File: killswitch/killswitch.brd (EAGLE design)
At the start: 42.3 x 42.3 mm, 32 parts, among them U1 CD4012BPWR, U2 2N7002-7-F

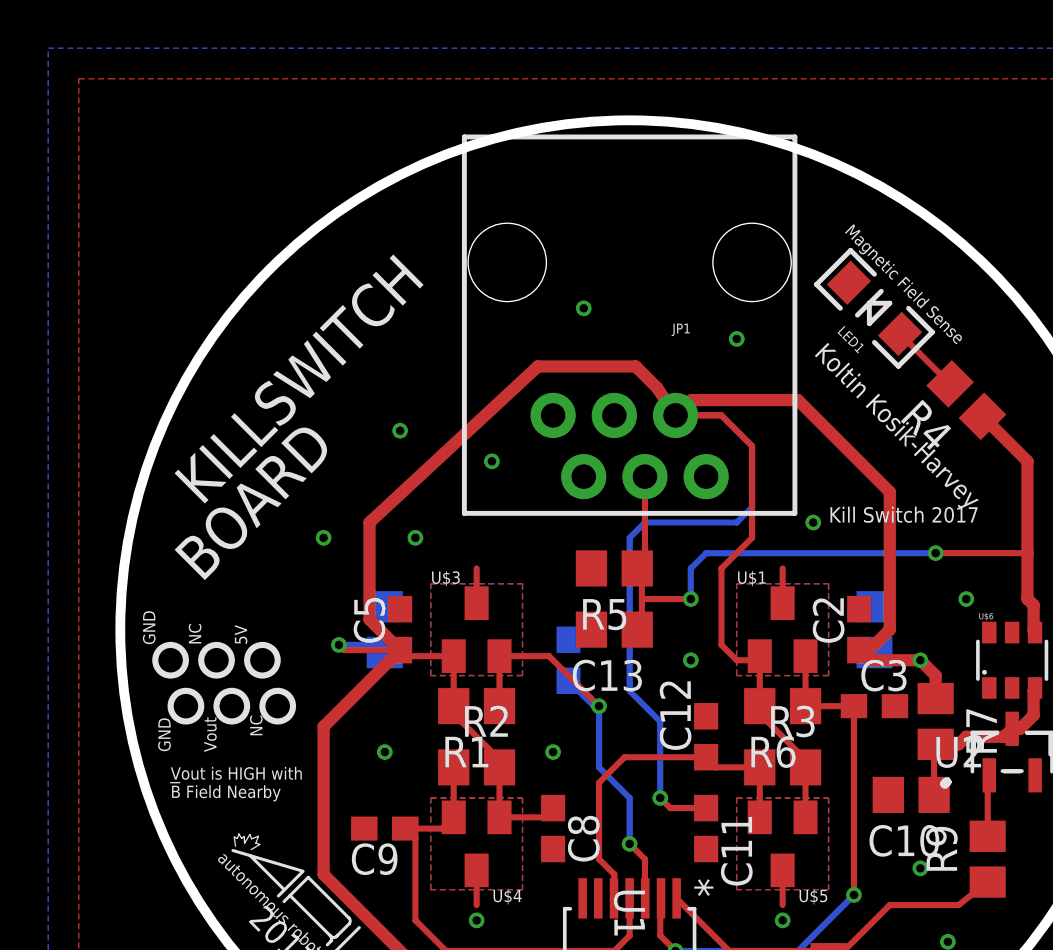
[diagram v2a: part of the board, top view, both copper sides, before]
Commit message: Removed RJ11 and replaced with 3-pin Header
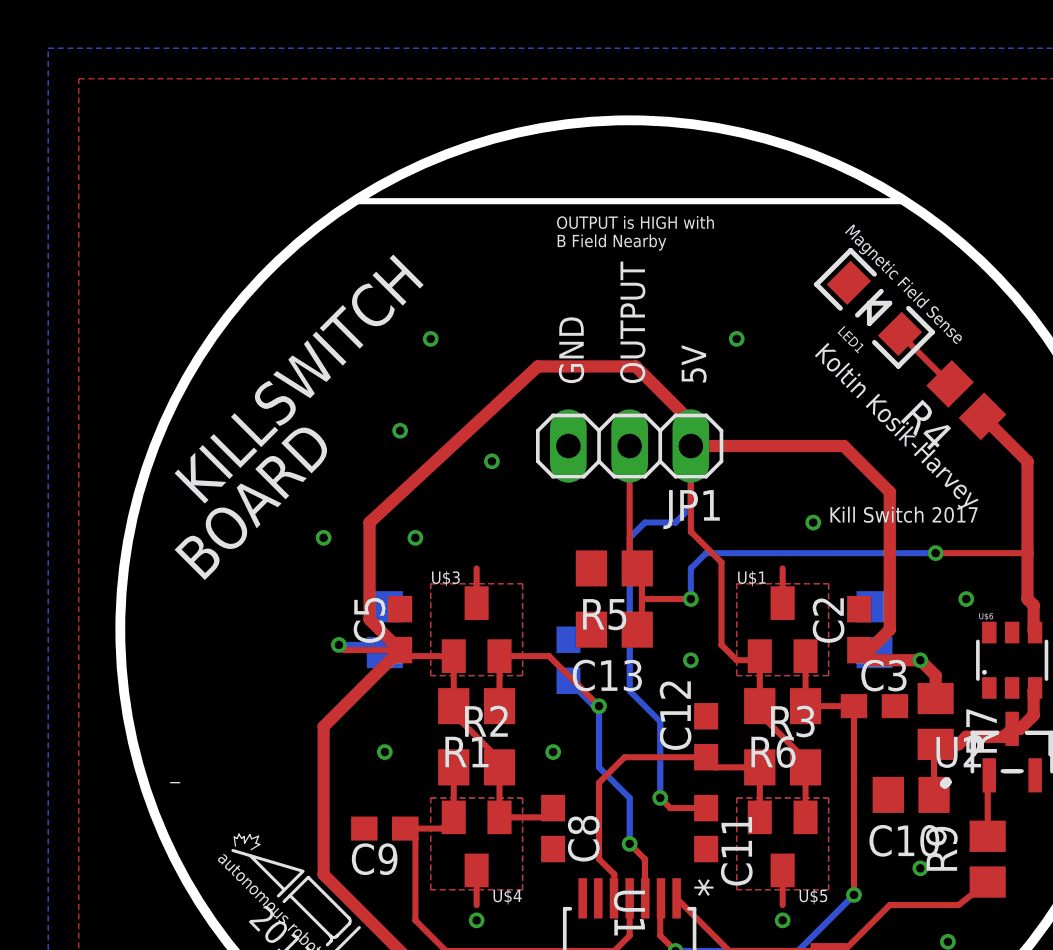
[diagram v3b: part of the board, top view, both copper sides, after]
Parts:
- JP1: value RJ11 -> (none); device SparkFun-Connectors:RJ11-6 -> pinhead:1X03
- moved JP1 7.62 mm to (20.3, 25.4)
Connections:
- net +5V: now also JP1.1; no longer JP1.2
- net GND: now also JP1.3; no longer JP1.5, JP1.6
- net OUTPUT: now also JP1.2; no longer JP1.3
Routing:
- net +5V: track 144.1 -> 134.1 mm
- net OUTPUT: track 34.5 -> 35.8 mm
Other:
- outline, holes or cut-outs redrawn
- board text added: "OUTPUT"
- board text added: "OUTPUT is HIGH with B Field Nearby"
- board text removed: "NC"
- board text removed: "Vout"
- board text removed: "Vout is HIGH with B Field Nearby"
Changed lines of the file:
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@@
 <text x="2.54" y="22.86" size="1.778" layer="21" font="vector" rot="R45">KILLSWITCH</text>
 <text x="2.54" y="19.685" size="1.778" layer="21" font="vector" rot="R45">BOARD</text>
-<circle x="1.27" y="16.51" radius="0.635" width="0.254" layer="21"/>
-<circle x="3.175" y="16.51" radius="0.635" width="0.254" layer="21"/>
-<circle x="5.08" y="16.51" radius="0.635" width="0.254" layer="21"/>
-<circle x="1.905" y="14.605" radius="0.635" width="0.254" layer="21"/>
-<circle x="3.81" y="14.605" radius="0.635" width="0.254" layer="21"/>
-<circle x="5.715" y="14.605" radius="0.635" width="0.254" layer="21"/>
-<text x="2.54" y="17.145" size="0.508" layer="21" rot="R90">NC</text>
-<text x="0.635" y="17.145" size="0.508" layer="21" rot="R90">GND</text>
-<text x="4.445" y="17.145" size="0.508" layer="21" rot="R90">5V</text>
-<text x="1.27" y="12.7" size="0.508" layer="21" rot="R90">GND</text>
-<text x="3.175" y="12.7" size="0.508" layer="21" rot="R90">Vout</text>
-<text x="5.08" y="13.335" size="0.508" layer="21" rot="R90">NC</text>
-<text x="1.27" y="10.795" size="0.508" layer="21">Vout is HIGH with
+<text x="23.495" y="27.94" size="1.016" layer="21" rot="R90">5V</text>
+<text x="18.415" y="27.94" size="1.016" layer="21" rot="R90">GND</text>
+<text x="20.955" y="27.94" size="1.016" layer="21" rot="R90">OUTPUT</text>
+<text x="17.272" y="33.655" size="0.508" layer="21">OUTPUT is HIGH with
 B Field Nearby</text>
 <wire x1="1.27" y1="11.43" x2="1.651" y2="11.43" width="0.0508" layer="21"/>
 <text x="29.21" y="34.29" size="0.508" layer="21" rot="R315">Magnetic Field Sense</text>
+<wire x1="8.89" y1="35.56" x2="31.75" y2="35.56" width="0.254" layer="20"/>
 </plain>
 <attributes>
@@
 </autorouter>
 <elements>
-<element name="JP1" library="SparkFun-Connectors" package="RJ11-6" value="RJ11" x="20.32" y="33.02" rot="R180">
-<attribute name="PROD_ID" value="CONN-08590" x="20.32" y="33.02" size="1.778" layer="27" rot="R180" display="off"/>
-<attribute name="VALUE" value="RJ11" x="20.32" y="33.02" size="1.778" layer="27" rot="R180" display="off"/>
-</element>
 <element name="U$2" library="ARVP" package="LOGO2" value="" x="3.175" y="8.255" smashed="yes" rot="R315"/>
 <element name="U$1" library="KillSwitch" library_urn="urn:adsk.eagle:library:576207" package="SOT23" value="TCS40DLR" x="26.67" y="17.78"/>
@@
 <element name="R9" library="resistor" library_urn="urn:adsk.eagle:library:348" package="R0805" package3d_urn="urn:adsk.eagle:package:26059/1" value="1k" x="35.179" y="8.255" rot="R90"/>
 <element name="C10" library="resistor" library_urn="urn:adsk.eagle:library:348" package="C0805" package3d_urn="urn:adsk.eagle:package:26137/1" value="100nF" x="32.004" y="10.922" rot="R180"/>
+<element name="JP1" library="pinhead" library_urn="urn:adsk.eagle:library:325" package="1X03" package3d_urn="urn:adsk.eagle:package:22458/2" value="" x="20.32" y="25.4" rot="R180"/>
 </elements>
 <signals>
 <signal name="GND">
-<contactref element="JP1" pad="5"/>
-<contactref element="JP1" pad="6"/>
 <contactref element="U$1" pad="GND"/>
 <contactref element="C1" pad="2"/>
@@
 <wire x1="26.67" y1="7.79" x2="26.67" y2="6.35" width="0.254" layer="1"/>
 <via x="11.43" y="21.59" extent="1-16" drill="0.35"/>
-<via x="18.415" y="31.115" extent="1-16" drill="0.35"/>
+<via x="12.065" y="29.845" extent="1-16" drill="0.35"/>
 <via x="27.94" y="22.225" extent="1-16" drill="0.35"/>
 <via x="38.735" y="21.59" extent="1-16" drill="0.35"/>
@@
 <contactref element="C13" pad="2"/>
 <contactref element="C10" pad="2"/>
+<contactref element="JP1" pad="3"/>
 </signal>
 <signal name="+5V">
-<contactref element="JP1" pad="2"/>
 <contactref element="U$1" pad="VCC"/>
 <contactref element="C1" pad="1"/>
@@
 <wire x1="25.72" y1="16.51" x2="25.72" y2="14.605" width="0.254" layer="1"/>
 <wire x1="25.72" y1="16.51" x2="25.72" y2="16.68" width="0.254" layer="1"/>
-<wire x1="22.225" y1="26.67" x2="24.13" y2="26.67" width="0.254" layer="1"/>
-<wire x1="24.13" y1="26.67" x2="25.4" y2="25.4" width="0.254" layer="1"/>
-<wire x1="25.4" y1="25.4" x2="25.4" y2="21.59" width="0.254" layer="1"/>
-<wire x1="25.4" y1="21.59" x2="24.13" y2="20.32" width="0.254" layer="1"/>
-<wire x1="24.13" y1="20.32" x2="24.13" y2="17.145" width="0.254" layer="1"/>
-<wire x1="24.13" y1="17.145" x2="24.765" y2="16.51" width="0.254" layer="1"/>
+<wire x1="24.765" y1="16.51" x2="24.13" y2="17.145" width="0.254" layer="1"/>
 <wire x1="24.765" y1="16.51" x2="25.72" y2="16.51" width="0.254" layer="1"/>
 <wire x1="27.62" y1="12.065" x2="27.62" y2="9.99" width="0.254" layer="1"/>
-<wire x1="22.225" y1="26.67" x2="21.463" y2="27.813" width="0.508" layer="1"/>
-<wire x1="21.463" y1="27.813" x2="20.574" y2="28.702" width="0.508" layer="1"/>
-<wire x1="20.574" y1="28.702" x2="16.51" y2="28.702" width="0.508" layer="1"/>
+<wire x1="16.51" y1="28.702" x2="20.574" y2="28.702" width="0.508" layer="1"/>
 <wire x1="9.525" y1="22.225" x2="9.525" y2="18.2" width="0.508" layer="1"/>
 <wire x1="9.525" y1="18.2" x2="10.795" y2="16.93" width="0.508" layer="1"/>
@@
 <wire x1="22.01" y1="10.375" x2="21.59" y2="10.795" width="0.254" layer="1"/>
 <via x="21.59" y="10.795" extent="1-16" drill="0.35"/>
-<wire x1="25.4" y1="22.86" x2="25.4" y2="25.4" width="0.254" layer="16"/>
-<wire x1="25.4" y1="25.4" x2="24.13" y2="26.67" width="0.254" layer="16"/>
-<wire x1="24.13" y1="26.67" x2="22.225" y2="26.67" width="0.254" layer="16"/>
 <wire x1="21.59" y1="10.795" x2="21.59" y2="13.97" width="0.254" layer="16"/>
 <wire x1="21.59" y1="13.97" x2="20.32" y2="15.24" width="0.254" layer="16"/>
 <wire x1="20.32" y1="15.24" x2="20.32" y2="21.59" width="0.254" layer="16"/>
 <wire x1="20.32" y1="21.59" x2="20.955" y2="22.225" width="0.254" layer="16"/>
-<wire x1="20.955" y1="22.225" x2="24.765" y2="22.225" width="0.254" layer="16"/>
-<wire x1="24.765" y1="22.225" x2="25.4" y2="22.86" width="0.254" layer="16"/>
 <via x="32.385" y="16.51" extent="1-16" drill="0.35"/>
 <wire x1="30.8" y1="16.51" x2="32.385" y2="16.51" width="0.254" layer="16"/>
@@
 <wire x1="14.92" y1="9.99" x2="16.76" y2="9.99" width="0.254" layer="1"/>
 <wire x1="16.76" y1="9.99" x2="17.145" y2="10.375" width="0.254" layer="1"/>
-<wire x1="27.305" y1="27.305" x2="22.86" y2="27.305" width="0.508" layer="1"/>
-<wire x1="22.86" y1="27.305" x2="22.225" y2="26.67" width="0.254" layer="1"/>
-<wire x1="31.115" y1="23.495" x2="27.305" y2="27.305" width="0.508" layer="1"/>
 <contactref element="U1" pad="14"/>
 <wire x1="7.62" y1="7.62" x2="16.51" y2="-1.27" width="0.508" layer="1"/>
@@
 <wire x1="32.385" y1="16.51" x2="33.02" y2="15.875" width="0.508" layer="1"/>
 <wire x1="33.02" y1="15.875" x2="33.02" y2="14.92" width="0.508" layer="1"/>
+<contactref element="JP1" pad="1"/>
+<wire x1="20.955" y1="22.225" x2="22.225" y2="22.225" width="0.254" layer="16"/>
+<wire x1="22.225" y1="22.225" x2="22.86" y2="22.86" width="0.254" layer="16"/>
+<wire x1="22.86" y1="22.86" x2="22.86" y2="25.4" width="0.254" layer="16"/>
+<wire x1="22.606" y1="26.67" x2="22.606" y2="25.654" width="0.508" layer="1"/>
+<wire x1="22.86" y1="25.4" x2="22.606" y2="25.654" width="0.508" layer="1"/>
+<wire x1="20.574" y1="28.702" x2="22.606" y2="26.67" width="0.508" layer="1"/>
+<wire x1="31.115" y1="23.495" x2="29.21" y2="25.4" width="0.508" layer="1"/>
+<wire x1="29.21" y1="25.4" x2="22.86" y2="25.4" width="0.508" layer="1"/>
+<wire x1="24.13" y1="20.574" x2="22.86" y2="21.844" width="0.254" layer="1"/>
+<wire x1="22.86" y1="21.844" x2="22.86" y2="25.4" width="0.254" layer="1"/>
+<wire x1="24.13" y1="17.145" x2="24.13" y2="20.574" width="0.254" layer="1"/>
 </signal>
 <signal name="N$5">
@@
 </signal>
 <signal name="OUTPUT">
-<contactref element="JP1" pad="3"/>
 <wire x1="33.02" y1="20.955" x2="36.83" y2="20.955" width="0.254" layer="1"/>
 <via x="33.02" y="20.955" extent="1-16" drill="0.35"/>
@@
 <wire x1="22.86" y1="20.32" x2="22.86" y2="19.05" width="0.254" layer="16"/>
 <via x="22.86" y="19.05" extent="1-16" drill="0.35"/>
-<wire x1="20.635" y1="23.81" x2="20.955" y2="24.13" width="0.254" layer="1"/>
 <contactref element="R4" pad="1"/>
 <wire x1="36.83" y1="24.764996875" x2="34.96175" y2="26.633246875" width="0.508" layer="1"/>
@@
 <wire x1="37.084" y1="17.721" x2="37.145" y2="17.66" width="0.508" layer="1"/>
 <wire x1="20.828" y1="20.127" x2="20.828" y2="19.05" width="0.254" layer="1"/>
-<wire x1="20.635" y1="20.32" x2="20.828" y2="20.127" width="0.254" layer="1"/>
+<wire x1="20.828" y1="20.127" x2="20.635" y2="20.32" width="0.254" layer="1"/>
 <wire x1="22.86" y1="19.05" x2="20.828" y2="19.05" width="0.254" layer="1"/>
 <wire x1="20.828" y1="19.05" x2="20.828" y2="17.973" width="0.254" layer="1"/>
 <wire x1="20.828" y1="17.973" x2="20.635" y2="17.78" width="0.254" layer="1"/>
-<wire x1="20.955" y1="24.13" x2="20.955" y2="20.64" width="0.254" layer="1"/>
 <wire x1="20.955" y1="20.64" x2="20.635" y2="20.32" width="0.254" layer="1"/>
+<contactref element="JP1" pad="2"/>
+<wire x1="20.635" y1="20.32" x2="20.635" y2="20.513" width="0.254" layer="1"/>
+<wire x1="20.635" y1="20.513" x2="20.32" y2="20.828" width="0.254" layer="1"/>
+<wire x1="20.32" y1="20.828" x2="20.32" y2="25.4" width="0.254" layer="1"/>
 </signal>
 <signal name="N$4">

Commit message: Minor tweaks to traces.
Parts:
- LED1: value (none) -> RED, 1.8V
- R4: value 320 -> 324
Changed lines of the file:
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@@
 <element name="C13" library="resistor" library_urn="urn:adsk.eagle:library:348" package="C0805" package3d_urn="urn:adsk.eagle:package:26137/1" value="2.2uF" x="19.685" y="17.78" rot="R180"/>
 <element name="C7" library="resistor" library_urn="urn:adsk.eagle:library:348" package="C0603" package3d_urn="urn:adsk.eagle:package:26138/1" value="1uF" x="24.13" y="0.635" rot="R90"/>
-<element name="R4" library="resistor" library_urn="urn:adsk.eagle:library:348" package="R0805" package3d_urn="urn:adsk.eagle:package:26059/1" value="320" x="34.29" y="27.305" rot="R135"/>
-<element name="LED1" library="SparkFun (2015_10_14 22_27_04 UTC)" package="LED-1206" value="" x="30.48" y="31.115" rot="R135"/>
+<element name="R4" library="resistor" library_urn="urn:adsk.eagle:library:348" package="R0805" package3d_urn="urn:adsk.eagle:package:26059/1" value="324" x="34.29" y="27.305" rot="R135"/>
+<element name="LED1" library="SparkFun (2015_10_14 22_27_04 UTC)" package="LED-1206" value="RED, 1.8V" x="30.48" y="31.115" rot="R135"/>
 <element name="U1" library="KillSwitch" library_urn="urn:adsk.eagle:library:576207" package="PW14" value="CD4012BPWR" x="20.32" y="3.81" rot="R270">
 <attribute name="MANUFACTURER_PART_NUMBER" value="CD4012BPWR" x="20.32" y="3.81" size="1.778" layer="27" rot="R270" display="off"/>
